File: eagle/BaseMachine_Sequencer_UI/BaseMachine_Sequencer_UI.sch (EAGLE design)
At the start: 12 parts, among them SW1 ALPS_SKHCBFA010, SW5 AK_TCTSW, SW6 AK_TCTSW

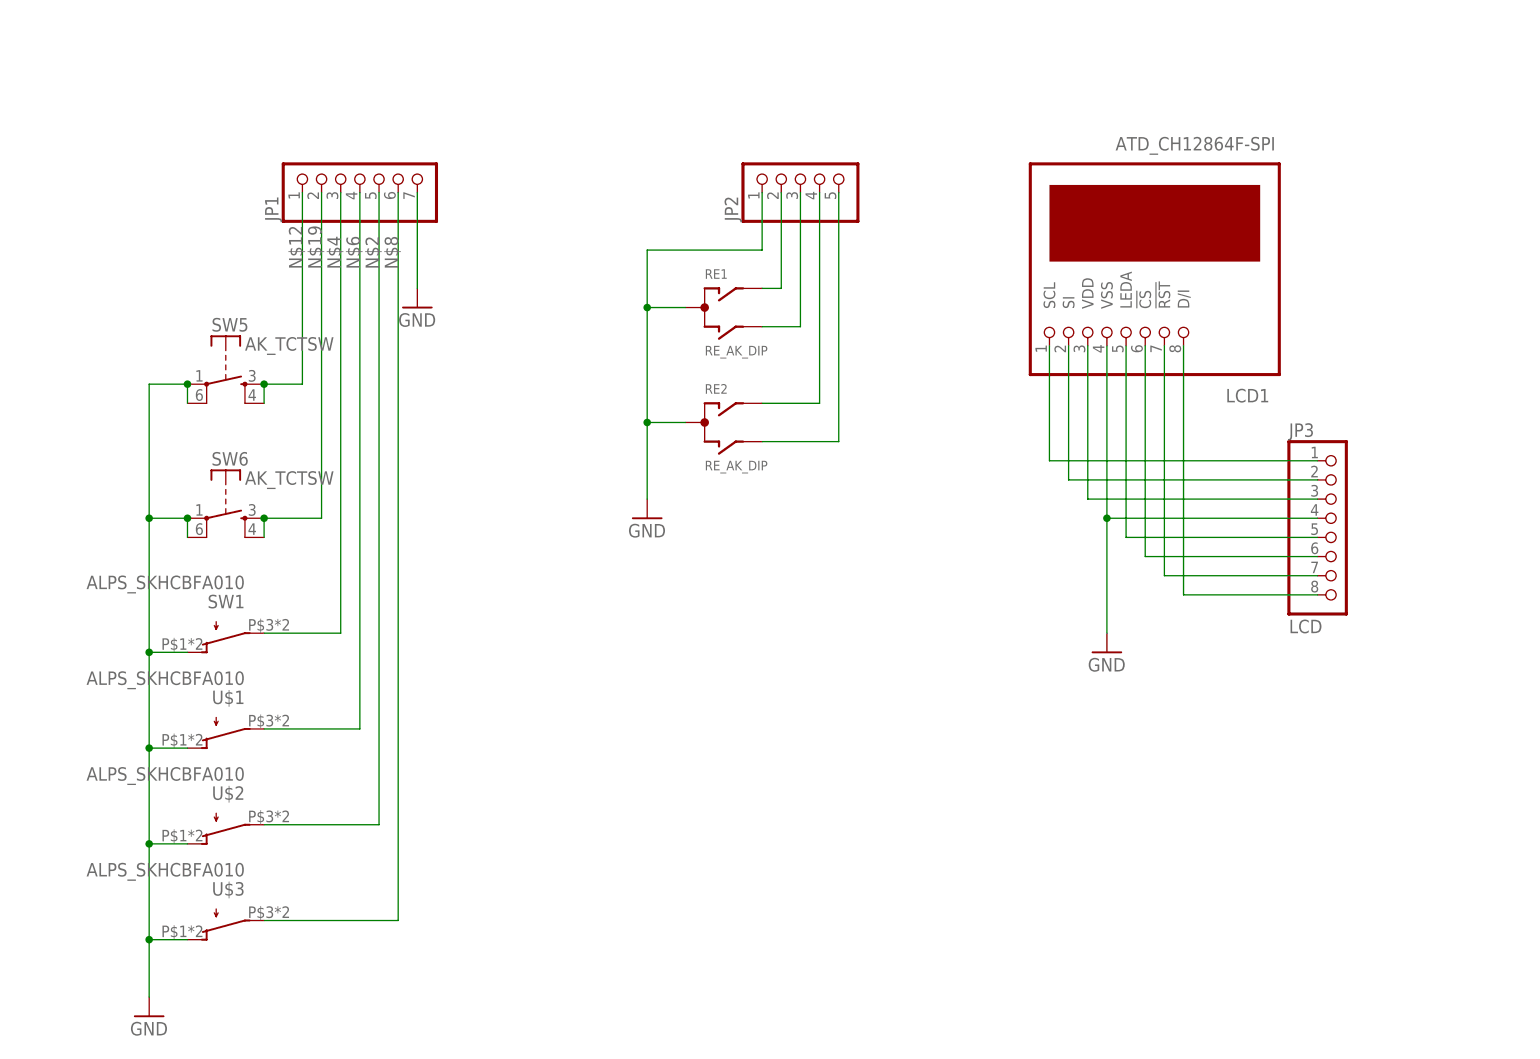
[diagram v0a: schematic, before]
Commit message: Update parts position
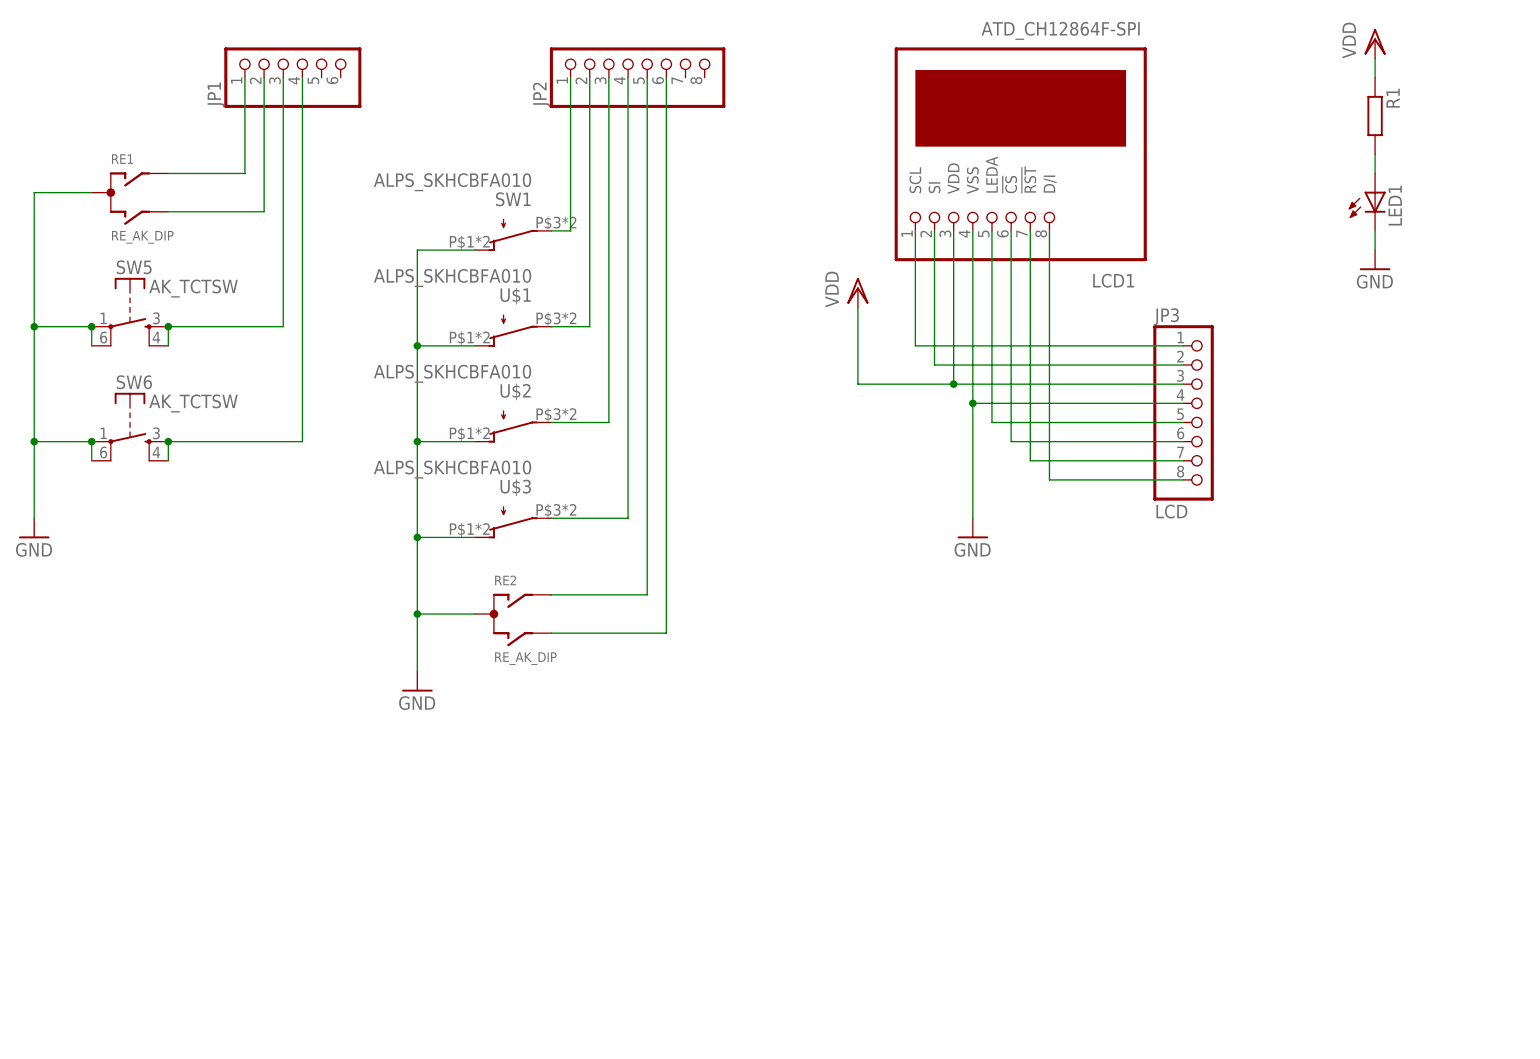
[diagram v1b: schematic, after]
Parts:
- added LED1: (no value), led:LED3MM
- added R1: (no value), rcl:R-EU_0207/7
- JP1: device pinhead:PINHD-1X7/90 -> pinhead:PINHD-1X6/90
- JP2: device pinhead:PINHD-1X5/90 -> pinhead:PINHD-1X8/90
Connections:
- removed net N$11: JP2.5, RE2.B
- removed net N$18: JP3.3, LCD1.VDD
- removed net N$5: JP2.3, RE1.B
- new net N$10: JP1.1, RE1.A
- new net N$13: JP1.2, RE1.B
- new net N$9: LED1.A, R1.2
- new net VDD: JP3.3, LCD1.VDD, R1.1
- net GND: now also LED1.C; no longer JP1.7, JP2.1
- net N$12: now also JP1.3; no longer JP1.1
- net N$19: now also JP1.4; no longer JP1.2
- net N$2: now also JP2.3; no longer JP1.5
- net N$3: now also JP2.6, RE2.B; no longer JP2.2, RE1.A
- net N$4: now also JP2.1; no longer JP1.3
- net N$6: now also JP2.2; no longer JP1.4
- net N$7: now also JP2.5; no longer JP2.4
- net N$8: now also JP2.4; no longer JP1.6
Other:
- moved on the sheet: JP3, LCD1, RE1, RE2, SW1, SW5, SW6, U$1, U$2, U$3

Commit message: routing
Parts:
- R1: value (none) -> 1k
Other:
- moved on the sheet: JP1, JP2, JP3, LCD1, LED1, R1, RE1, RE2, SW1, SW5, SW6, U$1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

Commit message: Update: UI & UI2 Board Design
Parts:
- removed LCD1: ATD_CH12864F-SPI, mylib2:ATD_CH12864F-SPI
- removed LED1: (no value), led:LED3MM
- removed R1: 1k, rcl:R-EU_0207/7
- added U$4: ATD_CH12864F-SPI, mylib2:ATD_CH12864F-SPI
- JP1: value (none) -> SW1
- JP2: value (none) -> SW2; device pinhead:PINHD-1X8/90 -> pinhead:PINHD-1X7/90
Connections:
- removed net N$1: JP3.1, LCD1.SCL
- removed net N$20: JP3.5, LCD1.LEDA
- removed net N$21: JP3.6, LCD1.!CS
- removed net N$7 (its old number): JP2.5, RE2.A
- new net LCD1: JP3.1, U$4.D/I
- new net N$3: JP2.7, RE2.A
- new net N$5: JP3.3, U$4.!CS
- net GND: now also JP1.5, JP2.1, JP3.5, U$4.VSS; no longer JP3.4, LCD1.VSS, LED1.C
- net N$10: now also RE1.B; no longer RE1.A
- net N$13: now also RE1.A; no longer RE1.B
- net N$17: now also U$4.!RST; no longer LCD1.SI
- net N$2: now also JP2.4; no longer JP2.3
- net N$22: now also U$4.SI; no longer LCD1.!RST
- net N$23: now also U$4.SCL; no longer LCD1.D/I
- net N$4: now also JP2.2; no longer JP2.1
- net N$6: now also JP2.3; no longer JP2.2
- net N$8: now also JP2.5; no longer JP2.4
- net N$9: now also JP3.4, U$4.LEDA; no longer LED1.A, R1.2
- net VDD: now also JP1.6, JP3.6, U$4.VDD; no longer JP3.3, LCD1.VDD, R1.1
